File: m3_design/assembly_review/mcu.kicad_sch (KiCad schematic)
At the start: 18 parts, among them J2 SWD+DFU 1x6, U1 STM32H743VIT6, Y1 25MHz CL8pF

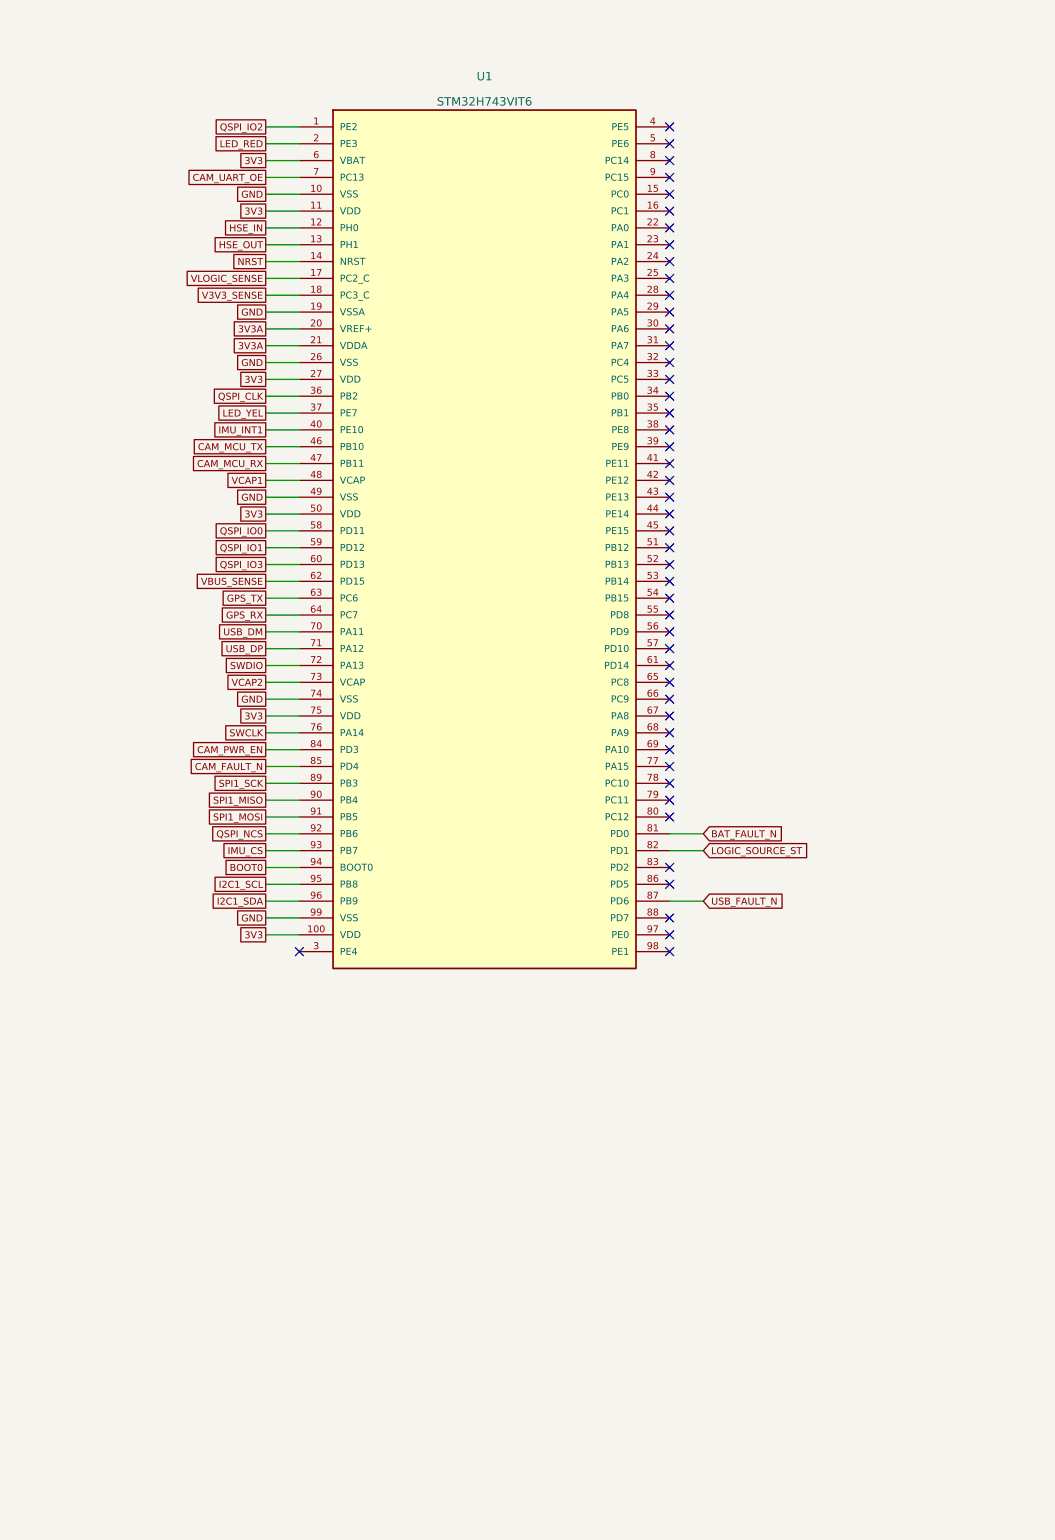
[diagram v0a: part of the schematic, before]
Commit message: M3-ASSY-R2: merge servos, dual fused pyro, arming, pull-pin and buzzer
Adds every remaining hardware function to the single M3 board (46 x 238 mm,
203 positions / 178 fitted parts, 14 sheets):

- Actuator power switch: back-to-back AON6403 from the battery input, gated
  by the U9 logic path so the one external switch still controls everything.
- Single-deploy dual pyro (owner ruling 2026-09-25): two AON7524 channels on
  two independently fused buses (FMEA H-5), separate 4-pos ARM and igniter
  terminals, per-bus arm sense, continuity, cold pull-up (H-1), gate networks
  per MARGIN_PRESCRIPTION P0-1/P0-2, PE3/PE6 sentinels (LED_RED -> PE8).
- Four servos (1 k series, pull-downs, SRV05-4), clamped pull-pin (PC14),
  MLT-8530 buzzer (PA5; pad mapping from the maker spec).
- Backup altimeter fully isolated by ruling: no interface on the board.
- New AON7524 footprint from AOS PO-00047 rev I; U12 LCSC code added.
- tools/export_fab.py (Gerber/drill zip, JLC BOM + CPL); m3_design/
  check_actuators.py (arming break / gate-network contract from PCB nets).

CAD checks only: tools/check.sh DRC 0 / unconnected 0 / parity 0 / ERC 0,
audit OK. No bench, simulation or flight evidence; no R2 firmware yet.

Co-Authored-By: Claude Opus 5.5 <noreply@anthropic.com>
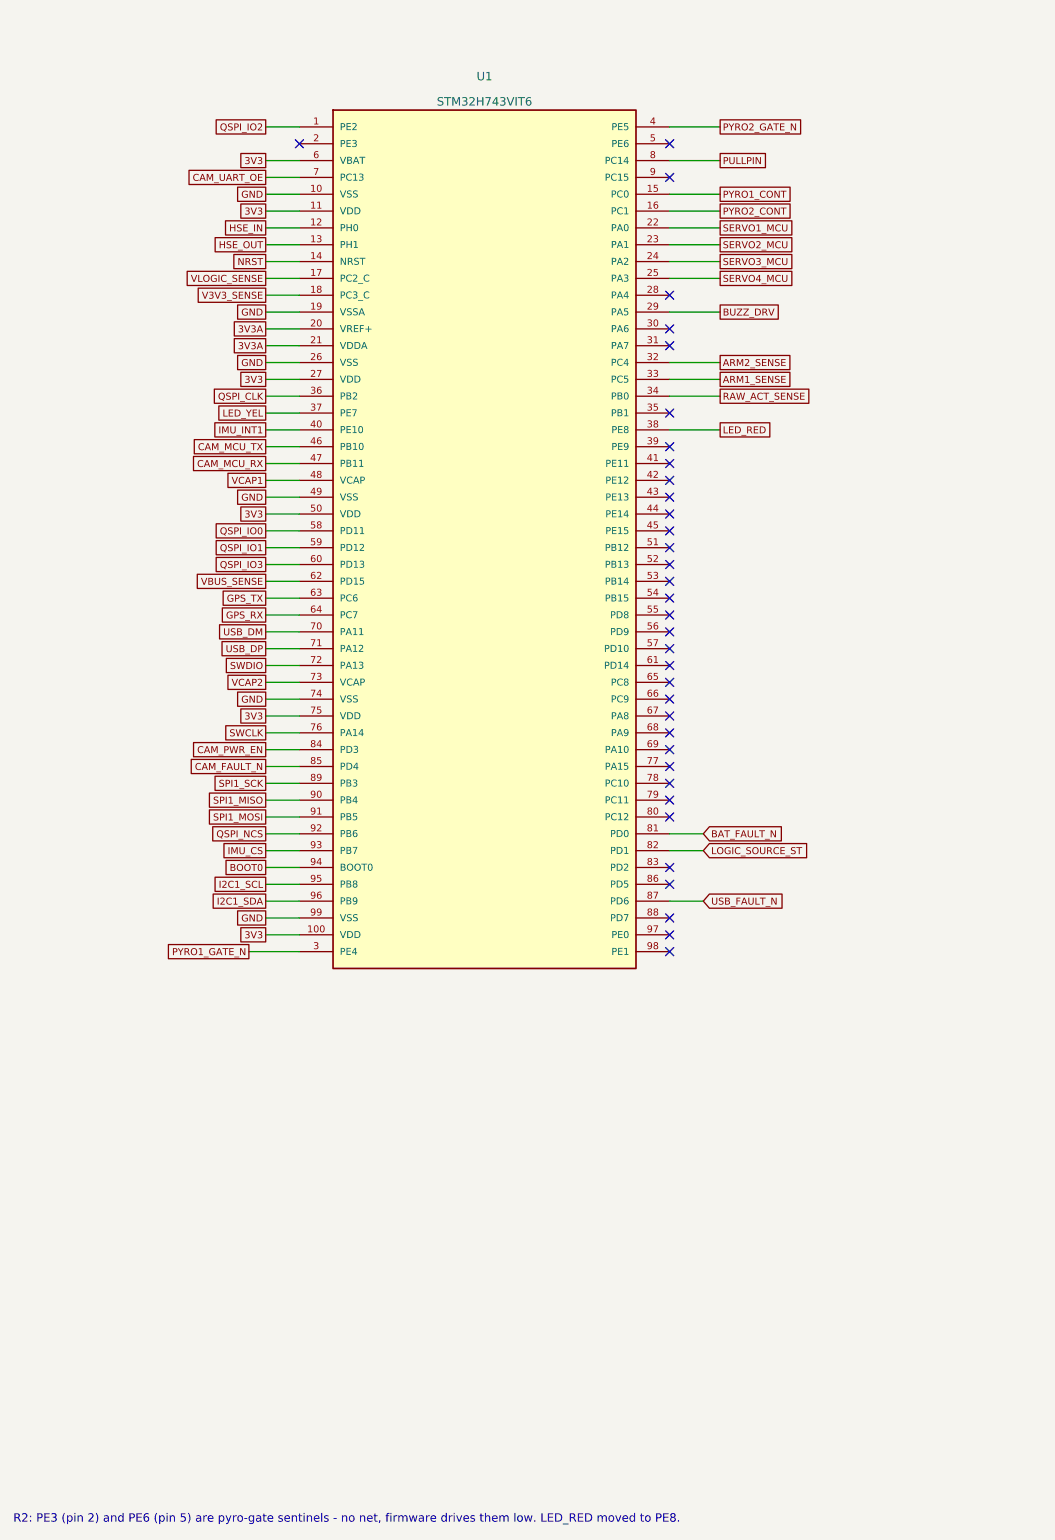
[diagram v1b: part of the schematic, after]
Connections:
- net LED_RED: now also U1.38 (PE8); no longer U1.2 (PE3)
- net PYRO1_CONT: now reaches U1.15 (PC0)
- net PYRO2_CONT: now reaches U1.16 (PC1)
- net SERVO1_MCU: now reaches U1.22 (PA0)
- net SERVO2_MCU: now reaches U1.23 (PA1)
- net SERVO3_MCU: now reaches U1.24 (PA2)
- net SERVO4_MCU: now reaches U1.25 (PA3)
- net BUZZ_DRV: now reaches U1.29 (PA5)
- net PYRO1_GATE_N: now reaches U1.3 (PE4)
- net ARM2_SENSE: now reaches U1.32 (PC4)
- net ARM1_SENSE: now reaches U1.33 (PC5)
- net RAW_ACT_SENSE: now reaches U1.34 (PB0)
- net PYRO2_GATE_N: now reaches U1.4 (PE5)
- net PULLPIN: now reaches U1.8 (PC14)
- no-connect marks 48 -> 35
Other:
- note added: "R2: PE3 (pin 2) and PE6 (pin 5) are pyro-gate sentinels - no net, firmware drives them low. LED_RED moved to PE8."
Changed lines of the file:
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@@
-	(wire
-		(pts
-			(xy 63.5 72.39)
-			(xy 58.42 72.39))
-		(stroke
-			(width 0)
-			(type default))
-)
-	(global_label "LED_RED"
-		(shape passive)
-		(at 58.42 72.39 0)
-		(effects
-			(font
-				(size 1.05 1.05))
-			(justify right))
-)
 	(wire
 		(pts
@@
 )
 	(no_connect
-		(at 63.5 194.31)
-)
-	(no_connect
-		(at 119.38 69.85)
-)
-	(no_connect
 		(at 119.38 72.39)
 )
 	(no_connect
-		(at 119.38 74.93)
-)
-	(no_connect
 		(at 119.38 77.47)
 )
 	(no_connect
-		(at 119.38 80.01)
-)
-	(no_connect
-		(at 119.38 82.55)
-)
-	(no_connect
-		(at 119.38 85.09)
-)
-	(no_connect
-		(at 119.38 87.63)
-)
-	(no_connect
-		(at 119.38 90.17)
-)
-	(no_connect
-		(at 119.38 92.71)
-)
-	(no_connect
 		(at 119.38 95.25)
 )
 	(no_connect
-		(at 119.38 97.79)
-)
-	(no_connect
 		(at 119.38 100.33)
 )
@@
 )
 	(no_connect
-		(at 119.38 105.41)
-)
-	(no_connect
-		(at 119.38 107.95)
-)
-	(no_connect
-		(at 119.38 110.49)
-)
-	(no_connect
 		(at 119.38 113.03)
-)
-	(no_connect
-		(at 119.38 115.57)
 )
 	(no_connect
@@
 		(effects
 			(font
+				(size 1.27 1.27))
+			(justify left))
+)
+	(wire
+		(pts
+			(xy 63.5 194.31)
+			(xy 55.88 194.31))
+		(stroke
+			(width 0)
+			(type default))
+)
+	(global_label "PYRO1_GATE_N"
+		(shape passive)
+		(at 55.88 194.31 180)
+		(effects
+			(font
+				(size 1.05 1.05))
+			(justify right))
+)
+	(wire
+		(pts
+			(xy 119.38 69.85)
+			(xy 127 69.85))
+		(stroke
+			(width 0)
+			(type default))
+)
+	(global_label "PYRO2_GATE_N"
+		(shape passive)
+		(at 127 69.85 0)
+		(effects
+			(font
+				(size 1.05 1.05))
+			(justify left))
+)
+	(wire
+		(pts
+			(xy 119.38 80.01)
+			(xy 127 80.01))
+		(stroke
+			(width 0)
+			(type default))
+)
+	(global_label "PYRO1_CONT"
+		(shape passive)
+		(at 127 80.01 0)
+		(effects
+			(font
+				(size 1.05 1.05))
+			(justify left))
+)
+	(wire
+		(pts
+			(xy 119.38 82.55)
+			(xy 127 82.55))
+		(stroke
+			(width 0)
+			(type default))
+)
+	(global_label "PYRO2_CONT"
+		(shape passive)
+		(at 127 82.55 0)
+		(effects
+			(font
+				(size 1.05 1.05))
+			(justify left))
+)
+	(wire
+		(pts
+			(xy 119.38 85.09)
+			(xy 127 85.09))
+		(stroke
+			(width 0)
+			(type default))
+)
+	(global_label "SERVO1_MCU"
+		(shape passive)
+		(at 127 85.09 0)
+		(effects
+			(font
+				(size 1.05 1.05))
+			(justify left))
+)
+	(wire
+		(pts
+			(xy 119.38 87.63)
+			(xy 127 87.63))
+		(stroke
+			(width 0)
+			(type default))
+)
+	(global_label "SERVO2_MCU"
+		(shape passive)
+		(at 127 87.63 0)
+		(effects
+			(font
+				(size 1.05 1.05))
+			(justify left))
+)
+	(wire
+		(pts
+			(xy 119.38 90.17)
+			(xy 127 90.17))
+		(stroke
+			(width 0)
+			(type default))
+)
+	(global_label "SERVO3_MCU"
+		(shape passive)
+		(at 127 90.17 0)
+		(effects
+			(font
+				(size 1.05 1.05))
+			(justify left))
+)
+	(wire
+		(pts
+			(xy 119.38 92.71)
+			(xy 127 92.71))
+		(stroke
+			(width 0)
+			(type default))
+)
+	(global_label "SERVO4_MCU"
+		(shape passive)
+		(at 127 92.71 0)
+		(effects
+			(font
+				(size 1.05 1.05))
+			(justify left))
+)
+	(wire
+		(pts
+			(xy 119.38 105.41)
+			(xy 127 105.41))
+		(stroke
+			(width 0)
+			(type default))
+)
+	(global_label "ARM2_SENSE"
+		(shape passive)
+		(at 127 105.41 0)
+		(effects
+			(font
+				(size 1.05 1.05))
+			(justify left))
+)
+	(wire
+		(pts
+			(xy 119.38 107.95)
+			(xy 127 107.95))
+		(stroke
+			(width 0)
+			(type default))
+)
+	(global_label "ARM1_SENSE"
+		(shape passive)
+		(at 127 107.95 0)
+		(effects
+			(font
+				(size 1.05 1.05))
+			(justify left))
+)
+	(wire
+		(pts
+			(xy 119.38 110.49)
+			(xy 127 110.49))
+		(stroke
+			(width 0)
+			(type default))
+)
+	(global_label "RAW_ACT_SENSE"
+		(shape passive)
+		(at 127 110.49 0)
+		(effects
+			(font
+				(size 1.05 1.05))
+			(justify left))
+)
+	(wire
+		(pts
+			(xy 119.38 115.57)
+			(xy 127 115.57))
+		(stroke
+			(width 0)
+			(type default))
+)
+	(global_label "LED_RED"
+		(shape passive)
+		(at 127 115.57 0)
+		(effects
+			(font
+				(size 1.05 1.05))
+			(justify left))
+)
+	(wire
+		(pts
+			(xy 119.38 97.79)
+			(xy 127 97.79))
+		(stroke
+			(width 0)
+			(type default))
+)
+	(global_label "BUZZ_DRV"
+		(shape passive)
+		(at 127 97.79 0)
+		(effects
+			(font
+				(size 1.05 1.05))
+			(justify left))
+)
+	(wire
+		(pts
+			(xy 119.38 74.93)
+			(xy 127 74.93))
+		(stroke
+			(width 0)
+			(type default))
+)
+	(global_label "PULLPIN"
+		(shape passive)
+		(at 127 74.93 0)
+		(effects
+			(font
+				(size 1.05 1.05))
+			(justify left))
+)
+	(no_connect
+		(at 63.5 72.39)
+)
+	(text "R2: PE3 (pin 2) and PE6 (pin 5) are pyro-gate sentinels - no net, firmware drives them low. LED_RED moved to PE8."
+		(at 20.32 280 0)
+		(effects
+			(font

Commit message: Make R2 orderable: stocked drop-ins, JLC placement corrections, ordering guide
- Stock (JLC assembly API): U8 AP63200 -> AP63300WU-7 (same TSOT26 pinout,
  VFB, fsw), L3 -> SRP5030T-6R8M (same body/land, AP63300 Table 1), C77
  100p -> 47p (Table 1), C84 25SVPF330M -> 35SVPK330M (same OS-CON F12).
  Every BOM line now has JLC stock for 5 boards except U6 SAM-M10Q
  (consign / Global Sourcing; DigiKey has stock).
- tools/jlc_orient.py matches each footprint pad-by-pad to the LCSC/EasyEDA
  footprint of its LCSC code; export_fab.py applies the rotation/offset.
  Without it U7, U8, U10, U11, U12, U13, D121 and LED2 would be rotated.
- tools/jlc_stock.py: repeatable stock check; fab/stock_check.json.
- JLC_Assembly field: U6 consign note, J2/J123 hand-cut from one 1x40 strip.
- docs/ORDERING.md: PCB options, PCBA, preview checklist, off-board parts.

DRC 0 / unconnected 0 / parity 0 / ERC 0, audit OK; contract OK;
tests 173/112/12 pass; sim 135 PASS.

Co-Authored-By: Claude Opus 5.5 (1M context) <noreply@anthropic.com>
Claude-Session: https://claude.ai/code/session_01DdkfTxR7SVyv9xZNmPk9vB
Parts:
- J2: JLC_Assembly (none) -> Hand: cut 1x6 from the 1x40 strip C2337 (one strip covers J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
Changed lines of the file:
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@@
+				(font
+					(size 1.27 1.27))))
+		(property "JLC_Assembly" "Hand: cut 1x6 from the 1x40 strip C2337 (one strip covers J2 and J123)"
+			(at 330.2 63.5 0)
+			(hide yes)
+			(effects
 				(font
 					(size 1.27 1.27))))

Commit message: Full PCBA: stocked J2/J123 headers, THT parts in the CPL with orientation corrections
- J2 -> PZ254V-11-06P (C492405), J123 -> PZ254V-11-02P (C492401); JLC cannot
  cut the former 1x40 strip.
- export_fab.py writes through-hole parts to the CPL (JLC THT assembly) and
  marks them 'THT (JLC THT assembly)'.
- jlc_corrections.json keyed by LCSC code + footprint (J1 and J9/J120/J121
  share C2915641 with two footprint variants); THT pad data added.
- ORDERING.md: full PCBA; U6 via JLC Global Sourcing or consignment.

DRC 0 / unconnected 0 / parity 0 / ERC 0, audit OK; contract OK; tests pass.

Co-Authored-By: Claude Opus 5.5 (1M context) <noreply@anthropic.com>
Claude-Session: https://claude.ai/code/session_01DdkfTxR7SVyv9xZNmPk9vB
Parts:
- J2: JLC_Assembly Hand: cut 1x6 from the 1x40 strip C2337 (one strip covers J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 -> (none); LCSC C2337 -> C492405; LCSC Part (none) -> C492405; Manufacturer (none) -> XFCN; Manufacturer Part (none) -> PZ254V-11-06P
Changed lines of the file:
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@@
 				(font
 					(size 1.27 1.27))))
-		(property "LCSC" "C2337"
+		(property "LCSC" "C492405"
 			(at 330.2 63.5 0)
 			(hide yes)
@@
 				(font
 					(size 1.27 1.27))))
-		(property "JLC_Assembly" "Hand: cut 1x6 from the 1x40 strip C2337 (one strip covers J2 and J123)"
+		(property "LCSC Part" "C492405"
 			(at 330.2 63.5 0)
 			(hide yes)
+			(effects
+				(font
+					(size 1.27 1.27))))
+		(property "Manufacturer" "XFCN"
+			(at 330.2 63.5 0)
+			(hide yes)
+			(effects
+				(font
+					(size 1.27 1.27))))
+		(property "Manufacturer Part" "PZ254V-11-06P"
+			(at 330.2 63.5 0)
+			(hide yes)

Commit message: Add CAM_5V sense (R104/R105/C94 -> PB1) so the USB self-test covers the camera regulator
AUTOTEST_DESIGN's sensing set is already on R2 (VLOGIC, 3V3, RAW_ACT, VBUS,
arm/continuity with cold pull-up, internal channels, buzzer load step); the
new camera branch had only a fault flag. CAM_5V x 1k/11k -> PB1 (ADC12_INP5):
0.477 V at 5.25 V, 1.40 V at the 15.4 V TVS clamp (< TT 4.0 V). Live only
while the board and the camera branch are powered, so no always-live path
into an unpowered MCU (AUTOTEST 2.4). Parts reuse existing LCSC codes.

Routed out from U1's outer side (0/45/90, 4 vias), no fan-out inside the
LQFP ring. DRC 0 / unconnected 0 / parity 0 / ERC 0, audit OK; tests pass;
CPL fully orientation-corrected; stock OK for 5 boards except U6.

Co-Authored-By: Claude Opus 5.5 (1M context) <noreply@anthropic.com>
Claude-Session: https://claude.ai/code/session_01DdkfTxR7SVyv9xZNmPk9vB
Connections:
- net CAM_5V_SENSE: now reaches U1.35 (PB1)
- no-connect marks 35 -> 34
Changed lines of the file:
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@@
-)
-	(no_connect
-		(at 119.38 113.03)
 )
 	(no_connect
@@
 			(type default))
 )
+	(wire
+		(pts
+			(xy 119.38 113.03)
+			(xy 127 113.03))
+		(stroke
+			(width 0)
+			(type default))
+)
+	(global_label "CAM_5V_SENSE"
+		(shape passive)
+		(at 127 113.03 0)
+		(effects
+			(font
+				(size 1.05 1.05))
+			(justify left))
+)
 	(global_label "RAW_ACT_SENSE"

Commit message: M3-ASSY-R3: remove GNSS, cut board to 46 x 193 mm
Schematic: U6/C33/C34 and GPS_TX/GPS_RX removed, PC6/PC7 no-connect, sheet 04
renamed, title-block revision R3 on all 14 sheets. PCB: m3_design/r3_cut.py deletes
227 tracks/vias (GPS nets, the U6-only 3V3A branch, forward GND stitching) and
U6/C33/C34; outline 46 x 193 mm, forward M3 pair moved to y = 189, GND zones
trimmed and refilled. No remaining track, via or footprint moved (checked
against R2). check.sh: DRC 0, unconnected 0, parity 0, ERC 0, audit OK;
check_actuators OK. Sheets, netlist, DRC/ERC evidence and renders regenerated.

Co-Authored-By: Claude Opus 5.5 <noreply@anthropic.com>
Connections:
- net GPS_RX: no longer names the net of U1.64 (PC7)
- net GPS_TX: no longer names the net of U1.63 (PC6)
- no-connect marks 34 -> 36
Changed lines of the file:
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@@
 		(title "02 | MCU, clock and debug")
 		(date "2026-09-07")
-		(rev "M3-ASSY-R1")
+		(rev "M3-ASSY-R3")
 		(company "Single-board M3 candidate; full system incomplete"))
 	(text "02 | MCU, clock and debug"
@@
 			(justify right))
 )
-	(wire
-		(pts
-			(xy 63.5 140.97)
-			(xy 58.42 140.97))
-		(stroke
-			(width 0)
-			(type default))
-)
-	(global_label "GPS_TX"
-		(shape passive)
-		(at 58.42 140.97 0)
-		(effects
-			(font
-				(size 1.05 1.05))
-			(justify right))
-)
-	(wire
-		(pts
-			(xy 63.5 143.51)
-			(xy 58.42 143.51))
-		(stroke
-			(width 0)
-			(type default))
-)
-	(global_label "GPS_RX"
-		(shape passive)
-		(at 58.42 143.51 0)
-		(effects
-			(font
-				(size 1.05 1.05))
-			(justify right))
-)
-	(wire
+	(no_connect
+		(at 63.5 140.97)
+)
+	(no_connect
+		(at 63.5 143.51)
+)
+	(wire
